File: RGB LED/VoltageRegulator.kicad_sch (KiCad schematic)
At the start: 3 parts, among them U1 AP2112K-3.3

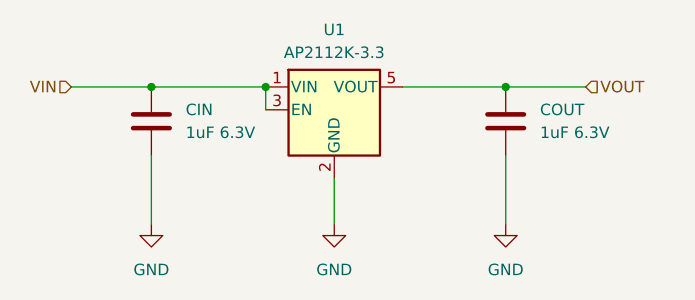
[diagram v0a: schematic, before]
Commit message: edited according to feedback
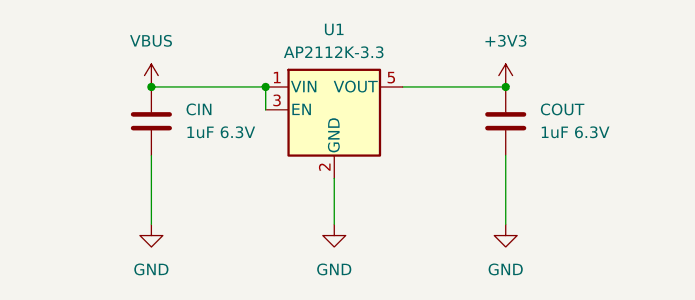
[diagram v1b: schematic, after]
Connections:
- net VIN renamed VBUS
- net VOUT renamed +3V3
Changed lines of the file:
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@@
-    (stroke (width 0) (type default))
-  )
-  (wire (pts (xy 90.17 77.47) (xy 99.06 77.47))
     (stroke (width 0) (type default))
   )
@@
   (wire (pts (xy 99.06 85.09) (xy 99.06 92.71))
     (stroke (width 0) (type default))
-  )
-  (wire (pts (xy 138.43 77.47) (xy 147.32 77.47))
-    (stroke (width 0) (type default))
-  )
-  (hierarchical_label "VIN" (shape input) (at 90.17 77.47 180) (fields_autoplaced)
-    (effects (font (size 1.27 1.27)) (justify right))
-  )
-  (hierarchical_label "VOUT" (shape input) (at 147.32 77.47 0) (fields_autoplaced)
-    (effects (font (size 1.27 1.27)) (justify left))
   )
   (symbol (lib_id "power:GND") (at 138.43 92.71 0) (unit 1)
@@
     )
   )
+  (symbol (lib_id "power:VBUS") (at 99.06 77.47 0) (unit 1)
+    (in_bom yes) (on_board yes) (dnp no) (fields_autoplaced)
+    (property "Reference" "#PWR015" (at 99.06 81.28 0)
+      (effects (font (size 1.27 1.27)) hide)
+    )
+    (property "Value" "VBUS" (at 99.06 72.39 0)
+      (effects (font (size 1.27 1.27)))
+    )
+    (property "Footprint" "" (at 99.06 77.47 0)
+      (effects (font (size 1.27 1.27)) hide)
+    )
+    (property "Datasheet" "" (at 99.06 77.47 0)
+      (effects (font (size 1.27 1.27)) hide)
+    )
+    (pin "1")
+    (instances
+      (project "RGB LED"
+        (path "/ac9a3c3e-b738-422c-8f43-94adc2643155/5a3cbc46-2a8b-41f0-a8f6-c2ea794ad112"
+          (reference "#PWR015") (unit 1)
+        )
+      )
+    )
+  )
   (symbol (lib_id "power:GND") (at 119.38 92.71 0) (unit 1)
     (in_bom yes) (on_board yes) (dnp no) (fields_autoplaced)
@@
         )
       )
+    )
+  )
+  (symbol (lib_id "power:+3V3") (at 138.43 77.47 0) (unit 1)
+    (in_bom yes) (on_board yes) (dnp no) (fields_autoplaced)
+    (property "Reference" "#PWR012" (at 138.43 81.28 0)
+      (effects (font (size 1.27 1.27)) hide)
+    )
+    (property "Value" "+3V3" (at 138.43 72.39 0)
+      (effects (font (size 1.27 1.27)))
+    )
+    (property "Footprint" "" (at 138.43 77.47 0)
+      (effects (font (size 1.27 1.27)) hide)
+    )
+    (property "Datasheet" "" (at 138.43 77.47 0)
+      (effects (font (size 1.27 1.27)) hide)
+    )
+    (pin "1")
+    (instances
+      (project "RGB LED"
+        (path "/ac9a3c3e-b738-422c-8f43-94adc2643155/5a3cbc46-2a8b-41f0-a8f6-c2ea794ad112"
+          (reference "#PWR012") (unit 1)
+        )
+      )

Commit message: added footprints
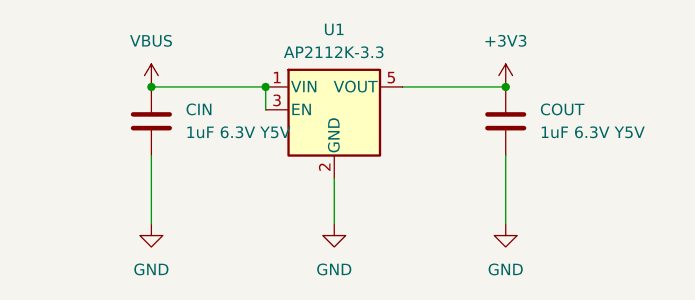
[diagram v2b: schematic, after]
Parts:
- CIN, COUT: value 1uF 6.3V -> 1uF 6.3V Y5V; footprint (none) -> Capacitor_SMD:C_0603_1608Metric
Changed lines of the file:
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@@
       (effects (font (size 1.27 1.27)) (justify left))
     )
-    (property "Value" "1uF 6.3V" (at 142.24 82.55 0)
+    (property "Value" "1uF 6.3V Y5V" (at 142.24 82.55 0)
       (effects (font (size 1.27 1.27)) (justify left))
     )
-    (property "Footprint" "" (at 139.3952 85.09 0)
+    (property "Footprint" "Capacitor_SMD:C_0603_1608Metric" (at 139.3952 85.09 0)
       (effects (font (size 1.27 1.27)) hide)
     )
@@
       (effects (font (size 1.27 1.27)) (justify left))
     )
-    (property "Value" "1uF 6.3V" (at 102.87 82.55 0)
+    (property "Value" "1uF 6.3V Y5V" (at 102.87 82.55 0)
       (effects (font (size 1.27 1.27)) (justify left))
     )
-    (property "Footprint" "" (at 100.0252 85.09 0)
+    (property "Footprint" "Capacitor_SMD:C_0603_1608Metric" (at 100.0252 85.09 0)
       (effects (font (size 1.27 1.27)) hide)
     )

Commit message: started layout
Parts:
- renumbered CIN to C5, COUT to C6
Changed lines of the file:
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@@
   (symbol (lib_id "Device:C") (at 138.43 81.28 0) (unit 1)
     (in_bom yes) (on_board yes) (dnp no) (fields_autoplaced)
-    (property "Reference" "COUT" (at 142.24 80.01 0)
+    (property "Reference" "C6" (at 142.24 80.01 0)
       (effects (font (size 1.27 1.27)) (justify left))
     )
@@
       (project "RGB LED"
         (path "/ac9a3c3e-b738-422c-8f43-94adc2643155/5a3cbc46-2a8b-41f0-a8f6-c2ea794ad112"
-          (reference "COUT") (unit 1)
+          (reference "C6") (unit 1)
         )
       )
@@
   (symbol (lib_id "Device:C") (at 99.06 81.28 0) (unit 1)
     (in_bom yes) (on_board yes) (dnp no) (fields_autoplaced)
-    (property "Reference" "CIN" (at 102.87 80.01 0)
+    (property "Reference" "C5" (at 102.87 80.01 0)
       (effects (font (size 1.27 1.27)) (justify left))
     )
@@
       (project "RGB LED"
         (path "/ac9a3c3e-b738-422c-8f43-94adc2643155/5a3cbc46-2a8b-41f0-a8f6-c2ea794ad112"
-          (reference "CIN") (unit 1)
+          (reference "C5") (unit 1)
         )
       )

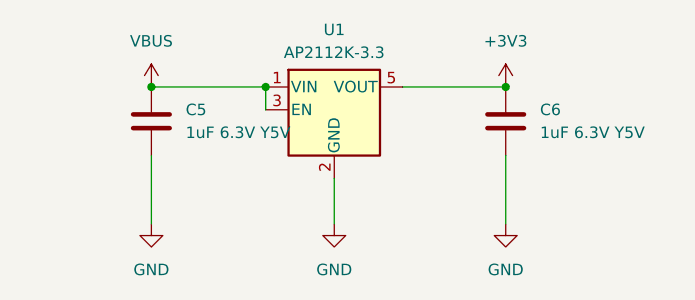
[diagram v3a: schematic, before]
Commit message: edited according to feedback
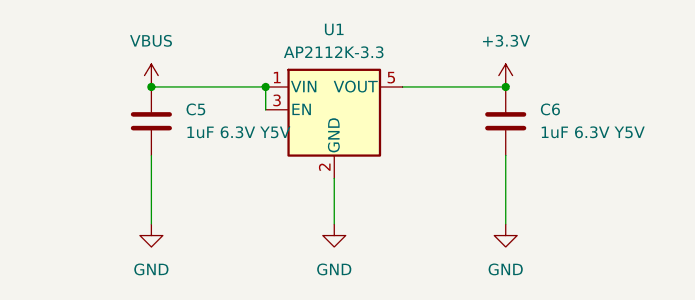
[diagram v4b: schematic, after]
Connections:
- net +3V3 renamed +3.3V
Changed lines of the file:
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@@
-    )
-  )
-  (symbol (lib_id "power:+3V3") (at 138.43 77.47 0) (unit 1)
-    (in_bom yes) (on_board yes) (dnp no) (fields_autoplaced)
-    (property "Reference" "#PWR012" (at 138.43 81.28 0)
-      (effects (font (size 1.27 1.27)) hide)
-    )
-    (property "Value" "+3V3" (at 138.43 72.39 0)
-      (effects (font (size 1.27 1.27)))
-    )
-    (property "Footprint" "" (at 138.43 77.47 0)
-      (effects (font (size 1.27 1.27)) hide)
-    )
-    (property "Datasheet" "" (at 138.43 77.47 0)
-      (effects (font (size 1.27 1.27)) hide)
-    )
-    (pin "1")
-    (instances
-      (project "RGB LED"
-        (path "/ac9a3c3e-b738-422c-8f43-94adc2643155/5a3cbc46-2a8b-41f0-a8f6-c2ea794ad112"
-          (reference "#PWR012") (unit 1)
-        )
-      )
     )
   )
@@
         )
       )
+    )
+  )
+  (symbol (lib_id "power:+3.3V") (at 138.43 77.47 0) (unit 1)
+    (in_bom yes) (on_board yes) (dnp no) (fields_autoplaced)
+    (property "Reference" "#PWR021" (at 138.43 81.28 0)
+      (effects (font (size 1.27 1.27)) hide)
+    )
+    (property "Value" "+3.3V" (at 138.43 72.39 0)
+      (effects (font (size 1.27 1.27)))
+    )
+    (property "Footprint" "" (at 138.43 77.47 0)
+      (effects (font (size 1.27 1.27)) hide)
+    )
+    (property "Datasheet" "" (at 138.43 77.47 0)
+      (effects (font (size 1.27 1.27)) hide)
+    )
+    (pin "1")
+    (instances
+      (project "RGB LED"
+        (path "/ac9a3c3e-b738-422c-8f43-94adc2643155/5a3cbc46-2a8b-41f0-a8f6-c2ea794ad112"
+          (reference "#PWR021") (unit 1)
+        )
+      )
